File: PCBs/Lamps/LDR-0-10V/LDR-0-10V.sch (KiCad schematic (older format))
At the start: 11 parts

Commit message: Add components values. Add PCB. Update project.
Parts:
- added D1: 1N4007, Diode_THT:D_DO-41_SOD81_P10.16mm_Horizontal, symbol Diode:1N4007
- added unit 2 of U1
- C1, C2, C3: renamed from C?; footprint (none) -> Capacitor_THT:C_Disc_D7.0mm_W2.5mm_P5.00mm
- J1: renamed from J?; value Conn_01x02_Female -> POWER; footprint (none) -> Connector_Phoenix_MSTB:PhoenixContact_MSTBA_2,5_2-G-5,08_1x02_P5.08mm_Horizontal
- J2: renamed from J?; value Conn_01x02_Female -> AO; footprint (none) -> Connector_Phoenix_MSTB:PhoenixContact_MSTBA_2,5_2-G-5,08_1x02_P5.08mm_Horizontal
- R1: renamed from R?; footprint OptoDevice:R_LDR_10x8.5mm_P7.6mm_Vertical -> OptoDevice:R_LDR_5.0x4.1mm_P3mm_Vertical
- R2: renamed from R?; value R -> 20k; footprint (none) -> Resistor_THT:R_Axial_DIN0207_L6.3mm_D2.5mm_P10.16mm_Horizontal
- R3: renamed from R?; value R -> 100; footprint Resistor_THT:R_Axial_DIN0414_L11.9mm_D4.5mm_P20.32mm_Horizontal -> Resistor_THT:R_Axial_DIN0207_L6.3mm_D2.5mm_P10.16mm_Horizontal
- RV1: renamed from RV?; value R_POT -> 5k; footprint (none) -> Potentiometer_THT:Potentiometer_ACP_CA9-V10_Vertical_Hole
- gave numbers to parts that had none: 1
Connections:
- net GND: now also U1.5 (+), U1.6 (-)
- net VCC: now also D1.1 (K); no longer J1.2 (Pin_2)
- new net: D1.2 (A), J1.2 (Pin_2)
- no-connect marks 0 -> 1
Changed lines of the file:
@@
 $EndDescr
 $Comp
-L Amplifier_Operational:LM358 U?
+L Amplifier_Operational:LM358 U1
 U 1 1 60893231
 P 7050 4000
-F 0 "U?" H 7050 4367 50  0000 C CNN
+F 0 "U1" H 7050 4367 50  0000 C CNN
 F 1 "LM358" H 7050 4276 50  0000 C CNN
 F 2 "Package_DIP:DIP-8_W7.62mm_LongPads" H 7050 4000 50  0001 C CNN
@@
 $EndComp
 $Comp
-L Amplifier_Operational:LM358 U?
+L Amplifier_Operational:LM358 U1
 U 3 1 60895EDF
 P 3800 4500
-F 0 "U?" H 3758 4546 50  0000 L CNN
+F 0 "U1" H 3758 4546 50  0000 L CNN
 F 1 "LM358" H 3758 4455 50  0000 L CNN
 F 2 "" H 3800 4500 50  0001 C CNN
@@
 $EndComp
 $Comp
-L Sensor_Optical:LDR03 R?
+L Sensor_Optical:LDR03 R1
 U 1 1 60898305
 P 5000 3500
-F 0 "R?" H 5070 3546 50  0000 L CNN
+F 0 "R1" H 5070 3546 50  0000 L CNN
 F 1 "LDR03" H 5070 3455 50  0000 L CNN
-F 2 "OptoDevice:R_LDR_10x8.5mm_P7.6mm_Vertical" V 5175 3500 50  0001 C CNN
+F 2 "OptoDevice:R_LDR_5.0x4.1mm_P3mm_Vertical" V 5175 3500 50  0001 C CNN
 F 3 "http://www.elektronica-componenten.nl/WebRoot/StoreNL/Shops/61422969/54F1/BA0C/C664/31B9/2173/C0A8/2AB9/2AEF/LDR03IMP.pdf" H 5000 3450 50  0001 C CNN
 	1    5000 3500
@@
 $EndComp
 $Comp
-L Device:R R?
+L Device:R R3
 U 1 1 60898D17
 P 7000 3500
-F 0 "R?" V 6793 3500 50  0000 C CNN
-F 1 "R" V 6884 3500 50  0000 C CNN
-F 2 "Resistor_THT:R_Axial_DIN0414_L11.9mm_D4.5mm_P20.32mm_Horizontal" V 6930 3500 50  0001 C CNN
+F 0 "R3" V 6793 3500 50  0000 C CNN
+F 1 "100" V 6884 3500 50  0000 C CNN
+F 2 "Resistor_THT:R_Axial_DIN0207_L6.3mm_D2.5mm_P10.16mm_Horizontal" V 6930 3500 50  0001 C CNN
 F 3 "~" H 7000 3500 50  0001 C CNN
 	1    7000 3500
@@
 $EndComp
 $Comp
-L Device:R R?
+L Device:R R2
 U 1 1 608995EB
 P 6500 4500
-F 0 "R?" H 6430 4454 50  0000 R CNN
-F 1 "R" H 6430 4545 50  0000 R CNN
-F 2 "" V 6430 4500 50  0001 C CNN
+F 0 "R2" H 6430 4454 50  0000 R CNN
+F 1 "20k" H 6430 4545 50  0000 R CNN
+F 2 "Resistor_THT:R_Axial_DIN0207_L6.3mm_D2.5mm_P10.16mm_Horizontal" V 6430 4500 50  0001 C CNN
 F 3 "~" H 6500 4500 50  0001 C CNN
 	1    6500 4500
@@
 	7350 4000 7500 4000
 $Comp
-L Device:C C?
+L Device:C C2
 U 1 1 6089C9CA
 P 6000 4500
-F 0 "C?" H 6115 4546 50  0000 L CNN
+F 0 "C2" H 6115 4546 50  0000 L CNN
 F 1 "100nF" H 6115 4455 50  0000 L CNN
-F 2 "" H 6038 4350 50  0001 C CNN
+F 2 "Capacitor_THT:C_Disc_D7.0mm_W2.5mm_P5.00mm" H 6038 4350 50  0001 C CNN
 F 3 "~" H 6000 4500 50  0001 C CNN
 	1    6000 4500
@@
 $EndComp
 $Comp
-L Device:C C?
+L Device:C C3
 U 1 1 6089D11C
 P 7500 4500
-F 0 "C?" H 7615 4546 50  0000 L CNN
+F 0 "C3" H 7615 4546 50  0000 L CNN
 F 1 "100nF" H 7615 4455 50  0000 L CNN
-F 2 "" H 7538 4350 50  0001 C CNN
+F 2 "Capacitor_THT:C_Disc_D7.0mm_W2.5mm_P5.00mm" H 7538 4350 50  0001 C CNN
 F 3 "~" H 7500 4500 50  0001 C CNN
 	1    7500 4500
@@
 $EndComp
 $Comp
-L Device:R_POT RV?
+L Device:R_POT RV1
 U 1 1 6089DFB3
 P 5000 4500
-F 0 "RV?" H 4931 4546 50  0000 R CNN
-F 1 "R_POT" H 4931 4455 50  0000 R CNN
-F 2 "" H 5000 4500 50  0001 C CNN
+F 0 "RV1" H 4931 4546 50  0000 R CNN
+F 1 "5k" H 4931 4455 50  0000 R CNN
+F 2 "Potentiometer_THT:Potentiometer_ACP_CA9-V10_Vertical_Hole" H 5000 4500 50  0001 C CNN
 F 3 "~" H 5000 4500 50  0001 C CNN
 	1    5000 4500
@@
 	6000 3900 5000 3900
 $Comp
-L Device:C C?
+L Device:C C1
 U 1 1 608AC229
 P 4250 4500
-F 0 "C?" H 4365 4546 50  0000 L CNN
+F 0 "C1" H 4365 4546 50  0000 L CNN
 F 1 "100nF" H 4365 4455 50  0000 L CNN
-F 2 "" H 4288 4350 50  0001 C CNN
+F 2 "Capacitor_THT:C_Disc_D7.0mm_W2.5mm_P5.00mm" H 4288 4350 50  0001 C CNN
 F 3 "~" H 4250 4500 50  0001 C CNN
 	1    4250 4500
@@
 	4250 3900 4250 4350
 $Comp
-L power:GND #PWR?
+L power:GND #PWR04
 U 1 1 608AE5FA
 P 5000 5100
-F 0 "#PWR?" H 5000 4850 50  0001 C CNN
+F 0 "#PWR04" H 5000 4850 50  0001 C CNN
 F 1 "GND" H 5005 4927 50  0000 C CNN
 F 2 "" H 5000 5100 50  0001 C CNN
@@
 Connection ~ 5000 5000
 $Comp
-L power:GND #PWR?
+L power:GND #PWR02
 U 1 1 608AF57D
 P 3700 5100
-F 0 "#PWR?" H 3700 4850 50  0001 C CNN
+F 0 "#PWR02" H 3700 4850 50  0001 C CNN
 F 1 "GND" H 3705 4927 50  0000 C CNN
 F 2 "" H 3700 5100 50  0001 C CNN
@@
 Connection ~ 3700 5000
 $Comp
-L power:VCC #PWR?
+L power:VCC #PWR01
 U 1 1 608B02DD
 P 3700 2900
-F 0 "#PWR?" H 3700 2750 50  0001 C CNN
+F 0 "#PWR01" H 3700 2750 50  0001 C CNN
 F 1 "VCC" H 3717 3073 50  0000 C CNN
 F 2 "" H 3700 2900 50  0001 C CNN
@@
 Connection ~ 3700 3900
 $Comp
-L power:VCC #PWR?
+L power:VCC #PWR03
 U 1 1 608B0CDA
 P 5000 2900
-F 0 "#PWR?" H 5000 2750 50  0001 C CNN
+F 0 "#PWR03" H 5000 2750 50  0001 C CNN
 F 1 "VCC" H 5017 3073 50  0000 C CNN
 F 2 "" H 5000 2900 50  0001 C CNN
@@
 	5500 5000 5000 5000
 $Comp
-L Connector:Conn_01x02_Female J?
+L Connector:Conn_01x02_Female J1
 U 1 1 608FC6EA
 P 2850 4550
-F 0 "J?" H 2742 4225 50  0000 C CNN
-F 1 "Conn_01x02_Female" H 2742 4316 50  0000 C CNN
-F 2 "" H 2850 4550 50  0001 C CNN
+F 0 "J1" H 2742 4225 50  0000 C CNN
+F 1 "POWER" H 2742 4316 50  0000 C CNN
+F 2 "Connector_Phoenix_MSTB:PhoenixContact_MSTBA_2,5_2-G-5,08_1x02_P5.08mm_Horizontal" H 2850 4550 50  0001 C CNN
 F 3 "~" H 2850 4550 50  0001 C CNN
 	1    2850 4550
@@
 $EndComp
 Wire Wire Line
-	3050 4450 3500 4450
-Wire Wire Line
-	3500 4450 3500 3900
-Wire Wire Line
-	3500 3900 3700 3900
-Wire Wire Line
-	3050 4550 3500 4550
-Wire Wire Line
-	3500 4550 3500 5000
-Wire Wire Line
-	3500 5000 3700 5000
-$Comp
-L Connector:Conn_01x02_Female J?
+	3050 4450 3200 4450
+Wire Wire Line
+	3200 4450 3200 4300
+Wire Wire Line
+	3050 4550 3200 4550
+Wire Wire Line
+	3200 4550 3200 5000
+Wire Wire Line
+	3200 5000 3700 5000
+$Comp
+L Connector:Conn_01x02_Female J2
 U 1 1 608FF72D
 P 8300 4000
-F 0 "J?" H 8328 3976 50  0000 L CNN
-F 1 "Conn_01x02_Female" H 8328 3885 50  0000 L CNN
-F 2 "" H 8300 4000 50  0001 C CNN
+F 0 "J2" H 8328 3976 50  0000 L CNN
+F 1 "AO" H 8328 3885 50  0000 L CNN
+F 2 "Connector_Phoenix_MSTB:PhoenixContact_MSTBA_2,5_2-G-5,08_1x02_P5.08mm_Horizontal" H 8300 4000 50  0001 C CNN
 F 3 "~" H 8300 4000 50  0001 C CNN
 	1    8300 4000
@@
 	8000 5000 7500 5000
 Connection ~ 7500 5000
+$Comp
+L Amplifier_Operational:LM358 U1
+U 2 1 609BD8EF
+P 7050 5850
+F 0 "U1" H 7050 6217 50  0000 C CNN
+F 1 "LM358" H 7050 6126 50  0000 C CNN
+F 2 "Package_DIP:DIP-8_W7.62mm_LongPads" H 7050 5850 50  0001 C CNN
+F 3 "http://www.ti.com/lit/ds/symlink/lm2904-n.pdf" H 7050 5850 50  0001 C CNN
+	2    7050 5850
+	1    0    0    -1
+$EndComp
+NoConn ~ 7350 5850
+$Comp
+L power:GND #PWR05
+U 1 1 609BF5D5
+P 6650 6150
+F 0 "#PWR05" H 6650 5900 50  0001 C CNN
+F 1 "GND" H 6655 5977 50  0000 C CNN
+F 2 "" H 6650 6150 50  0001 C CNN
+F 3 "" H 6650 6150 50  0001 C CNN
+	1    6650 6150
+	1    0    0    -1
+$EndComp
+Wire Wire Line
+	6750 5950 6650 5950
+Wire Wire Line
+	6650 5950 6650 6150
+Wire Wire Line
+	6750 5750 6650 5750
+Wire Wire Line
+	6650 5750 6650 5950
+Connection ~ 6650 5950
+$Comp
+L Diode:1N4007 D1
+U 1 1 609CDDEE
+P 3200 4150
+F 0 "D1" V 3154 4229 50  0000 L CNN
+F 1 "1N4007" V 3245 4229 50  0000 L CNN
+F 2 "Diode_THT:D_DO-41_SOD81_P10.16mm_Horizontal" H 3200 3975 50  0001 C CNN
+F 3 "http://www.vishay.com/docs/88503/1n4001.pdf" H 3200 4150 50  0001 C CNN
+	1    3200 4150
+	0    1    1    0
+$EndComp
+Wire Wire Line
+	3200 3900 3200 4000
+Wire Wire Line
+	3200 3900 3700 3900
 $EndSCHEMATC

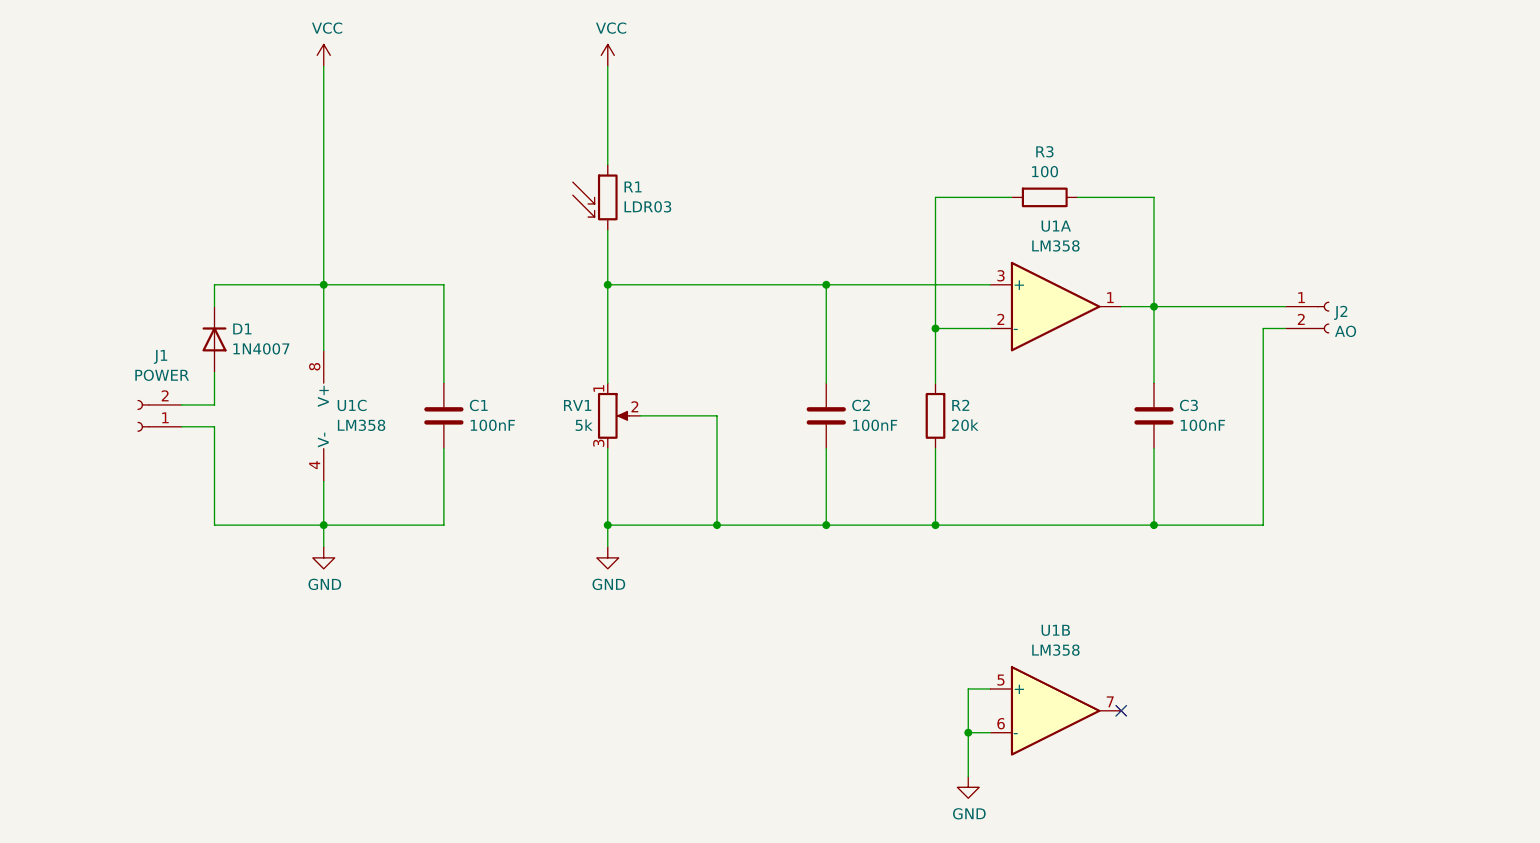
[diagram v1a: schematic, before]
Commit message: General modification beacuse of dome light inflector
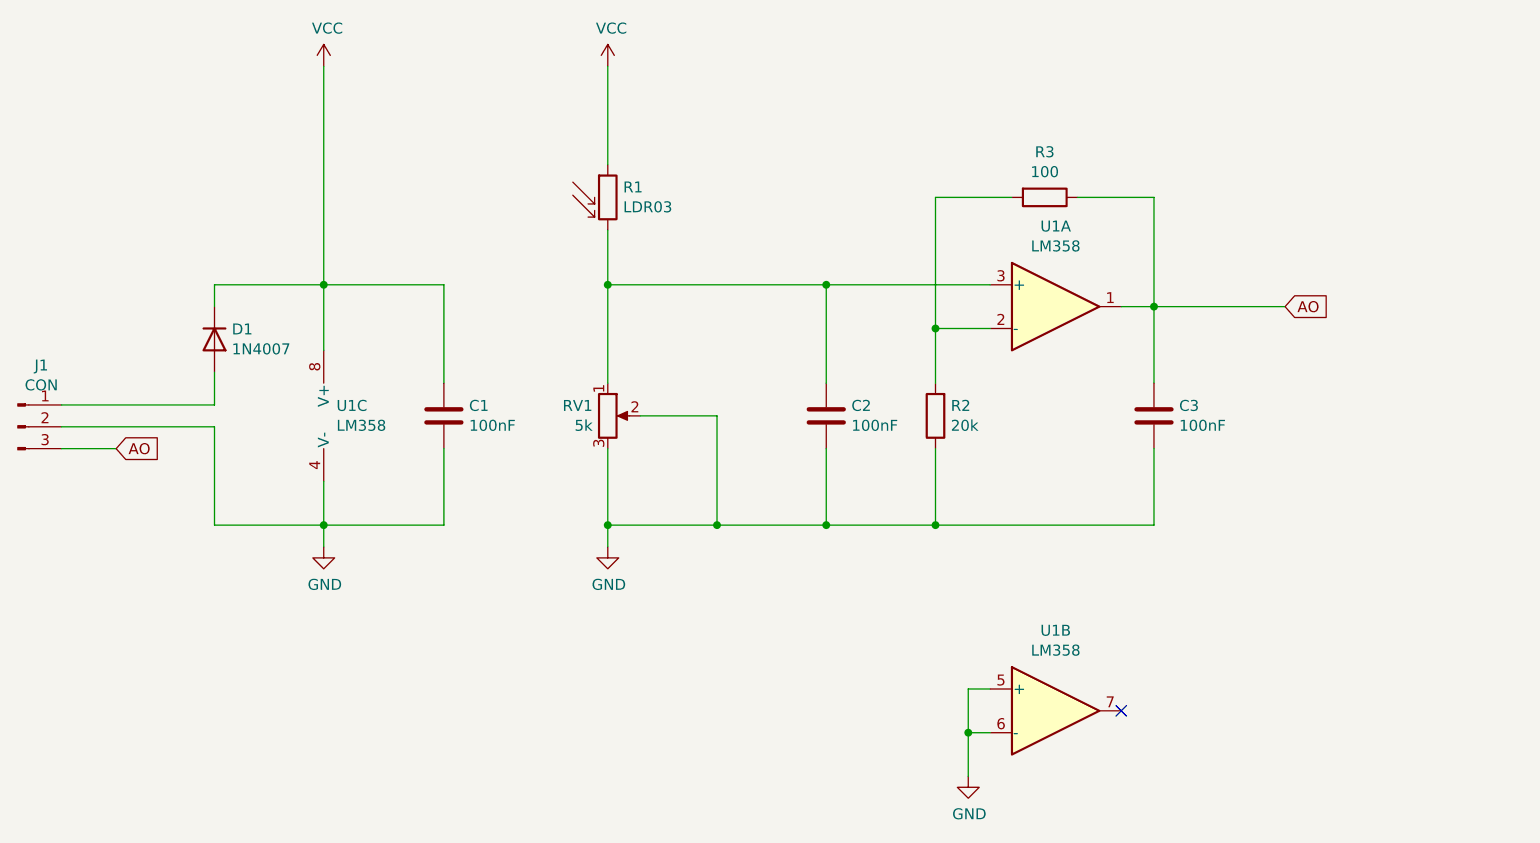
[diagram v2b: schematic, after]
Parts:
- removed J1: POWER, Connector_Phoenix_MSTB:PhoenixContact_MSTBA_2,5_2-G-5,08_1x02_P5.08mm_Horizontal, symbol Connector:Conn_01x02_Female
- removed J2: AO, Connector_Phoenix_MSTB:PhoenixContact_MSTBA_2,5_2-G-5,08_1x02_P5.08mm_Horizontal, symbol Connector:Conn_01x02_Female
- added J1: CON, Connector_Phoenix_MSTB:PhoenixContact_MSTBA_2,5_3-G-5,08_1x03_P5.08mm_Horizontal, symbol Connector:Conn_01x03_Male
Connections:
- net GND: now also J1.2 (Pin_2)
- net AO: now reaches C3.1, R3.1, U1.1
- net AO: now also J1.3 (Pin_3)
- net at D1.2 (A): now also J1.1 (Pin_1)
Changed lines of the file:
@@
 Wire Wire Line
 	5500 5000 5000 5000
-$Comp
-L Connector:Conn_01x02_Female J1
-U 1 1 608FC6EA
-P 2850 4550
-F 0 "J1" H 2742 4225 50  0000 C CNN
-F 1 "POWER" H 2742 4316 50  0000 C CNN
-F 2 "Connector_Phoenix_MSTB:PhoenixContact_MSTBA_2,5_2-G-5,08_1x02_P5.08mm_Horizontal" H 2850 4550 50  0001 C CNN
-F 3 "~" H 2850 4550 50  0001 C CNN
-	1    2850 4550
-	-1   0    0    1
-$EndComp
 Wire Wire Line
-	3050 4450 3200 4450
+	2500 4450 3200 4450
 Wire Wire Line
 	3200 4450 3200 4300
 Wire Wire Line
-	3050 4550 3200 4550
+	2500 4550 3200 4550
 Wire Wire Line
 	3200 4550 3200 5000
 Wire Wire Line
 	3200 5000 3700 5000
-$Comp
-L Connector:Conn_01x02_Female J2
-U 1 1 608FF72D
-P 8300 4000
-F 0 "J2" H 8328 3976 50  0000 L CNN
-F 1 "AO" H 8328 3885 50  0000 L CNN
-F 2 "Connector_Phoenix_MSTB:PhoenixContact_MSTBA_2,5_2-G-5,08_1x02_P5.08mm_Horizontal" H 8300 4000 50  0001 C CNN
-F 3 "~" H 8300 4000 50  0001 C CNN
-	1    8300 4000
-	1    0    0    -1
-$EndComp
 Wire Wire Line
 	8100 4000 7500 4000
-Wire Wire Line
-	8100 4100 8000 4100
-Wire Wire Line
-	8000 4100 8000 5000
-Wire Wire Line
-	8000 5000 7500 5000
-Connection ~ 7500 5000
 $Comp
 L Amplifier_Operational:LM358 U1
@@
 Wire Wire Line
 	3200 3900 3700 3900
+Text GLabel 8100 4000 2    50   Input ~ 0
+AO
+$Comp
+L Connector:Conn_01x03_Male J1
+U 1 1 60A470FC
+P 2300 4550
+F 0 "J1" H 2408 4831 50  0000 C CNN
+F 1 "CON" H 2408 4740 50  0000 C CNN
+F 2 "Connector_Phoenix_MSTB:PhoenixContact_MSTBA_2,5_3-G-5,08_1x03_P5.08mm_Horizontal" H 2300 4550 50  0001 C CNN
+F 3 "~" H 2300 4550 50  0001 C CNN
+	1    2300 4550
+	1    0    0    -1
+$EndComp
+Text GLabel 2750 4650 2    50   Input ~ 0
+AO
+Wire Wire Line
+	2500 4650 2750 4650
 $EndSCHEMATC

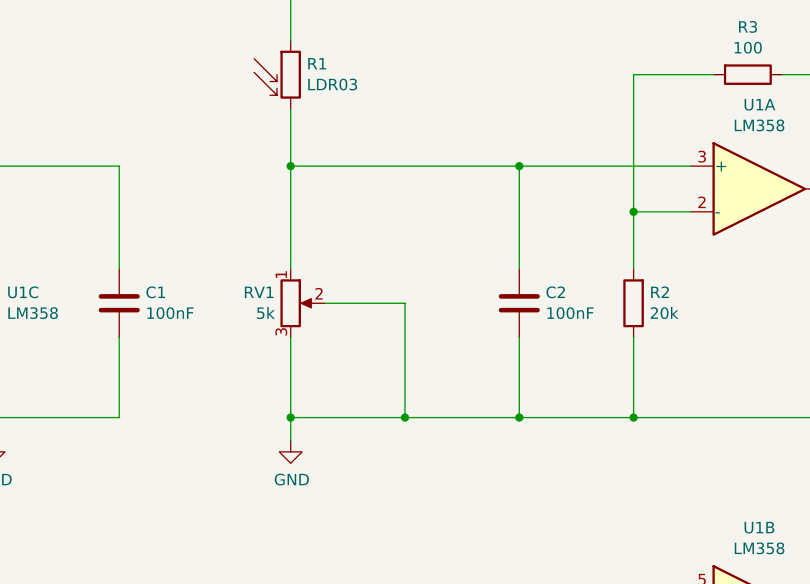
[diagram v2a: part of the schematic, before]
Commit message: Update LDR-0-10V
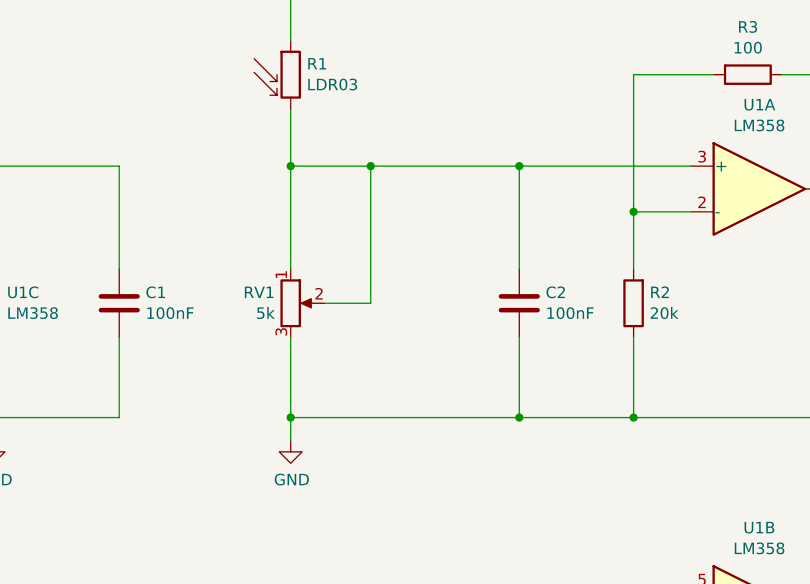
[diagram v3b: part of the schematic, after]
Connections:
- net GND: no longer RV1.2
- net at C2.1, R1.2, RV1.1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: now also RV1.2
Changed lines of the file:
@@
 	6750 3900 6000 3900
 Wire Wire Line
-	5000 3900 5000 4350
-Wire Wire Line
 	5000 3900 5000 3650
-Connection ~ 5000 3900
 Wire Wire Line
 	7500 4000 7500 4350
@@
 Connection ~ 6000 5000
 Wire Wire Line
-	6000 5000 5500 5000
-Wire Wire Line
 	6500 4650 6500 5000
 Connection ~ 6500 5000
@@
 Connection ~ 6000 3900
 Wire Wire Line
-	6000 3900 5000 3900
+	6000 3900 5350 3900
 $Comp
 L Device:C C1
@@
 	5000 3350 5000 2900
 Wire Wire Line
-	5150 4500 5500 4500
-Wire Wire Line
-	5500 4500 5500 5000
-Connection ~ 5500 5000
-Wire Wire Line
-	5500 5000 5000 5000
-Wire Wire Line
 	2500 4450 3200 4450
 Wire Wire Line
@@
 Wire Wire Line
 	2500 4650 2750 4650
+Wire Wire Line
+	5000 5000 6000 5000
+Wire Wire Line
+	5350 4500 5150 4500
+Connection ~ 5000 3900
+Connection ~ 5350 3900
+Wire Wire Line
+	5350 3900 5000 3900
+Wire Wire Line
+	5000 3900 5000 4350
+Wire Wire Line
+	5350 3900 5350 4500
 $EndSCHEMATC
